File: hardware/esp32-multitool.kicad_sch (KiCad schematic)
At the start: 0 parts

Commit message: block refactoring
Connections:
- no-connect marks 2 -> 0
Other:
- sheet analog_io renamed analog_in
- sheet digital_io renamed digital_in
- sheet 1wire ports: added 1WIRE_3V3, 1WIRE_DQ; removed none
- sheet analog_in ports: added AIN1, AIN2; removed none
- sheet canbus ports: added none; removed +3.3V, CAN_RX, CAN_TX, GND, VIN
- sheet digital_in ports: added DIN1, DIN2; removed none
- sheet esp32 ports: added 1WIRE_DQ, AIN1, AIN2, DIN1, DIN2, I2C_SCL, I2C_SDA, PWM1; removed CAN_RX, CAN_TX, GND, LEDC1
- sheet i2c ports: added I2C_3V3, I2C_GND, I2C_SCL, I2C_SDA; removed none
- sheet power: file power.kicad_sch -> blocks/AOZ1280CI/AOZ1280CI.kicad_sch
- sheet power ports: added VIN_PROTECTED; removed +3.3V, GND, USB_5V, VIN
- sheet pwm ports: added PWM1, VIN_PROTECTED; removed none

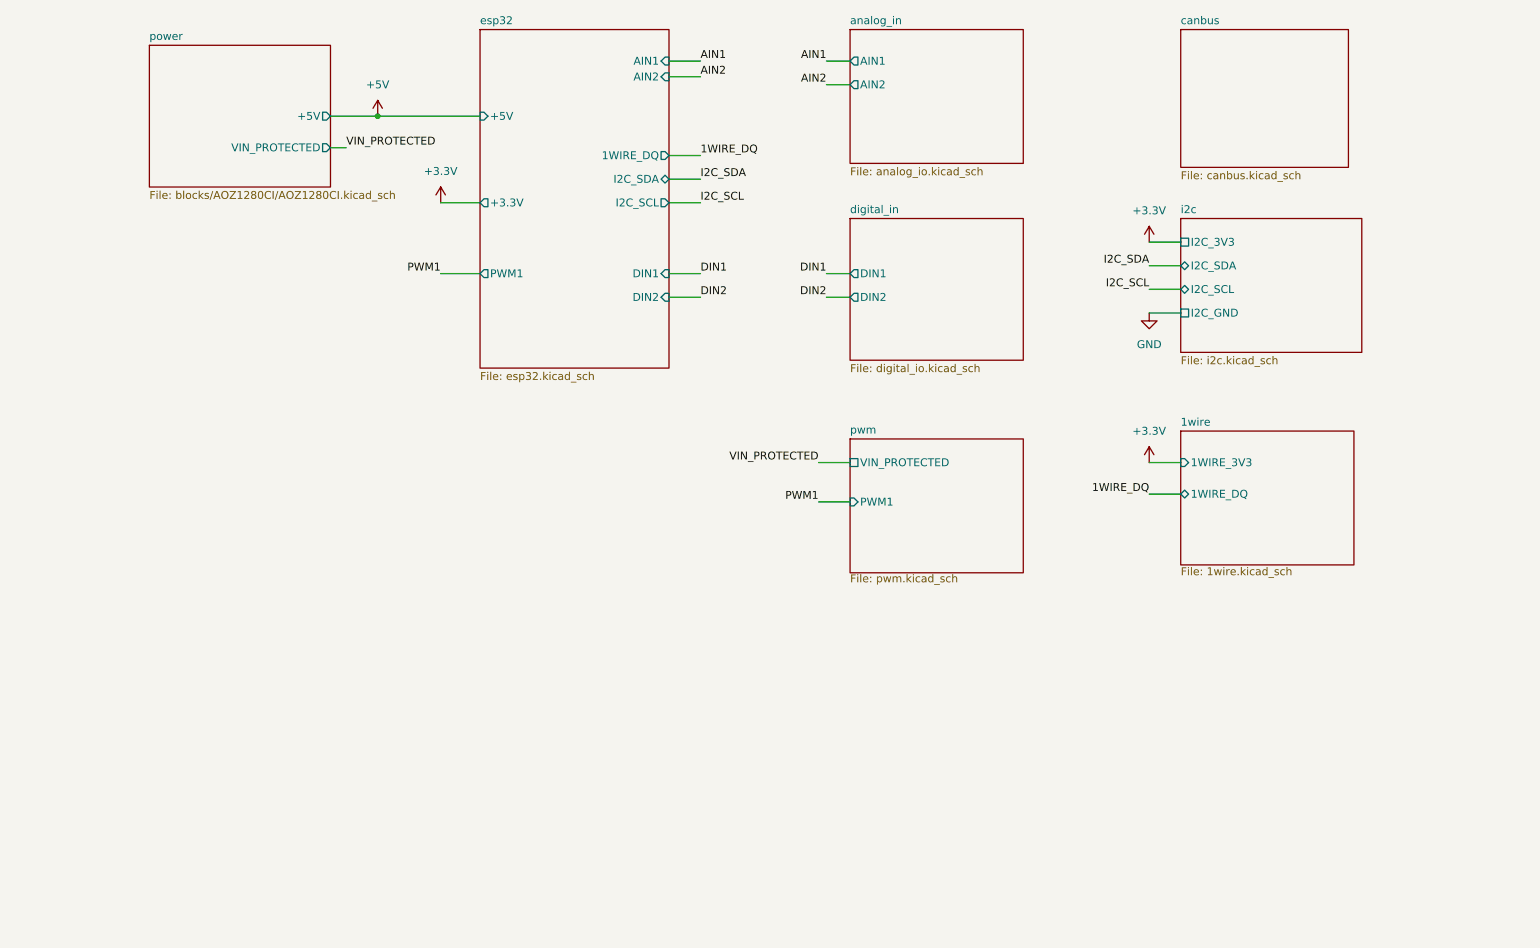
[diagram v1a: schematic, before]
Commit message: Added 3D models and ran freerouting
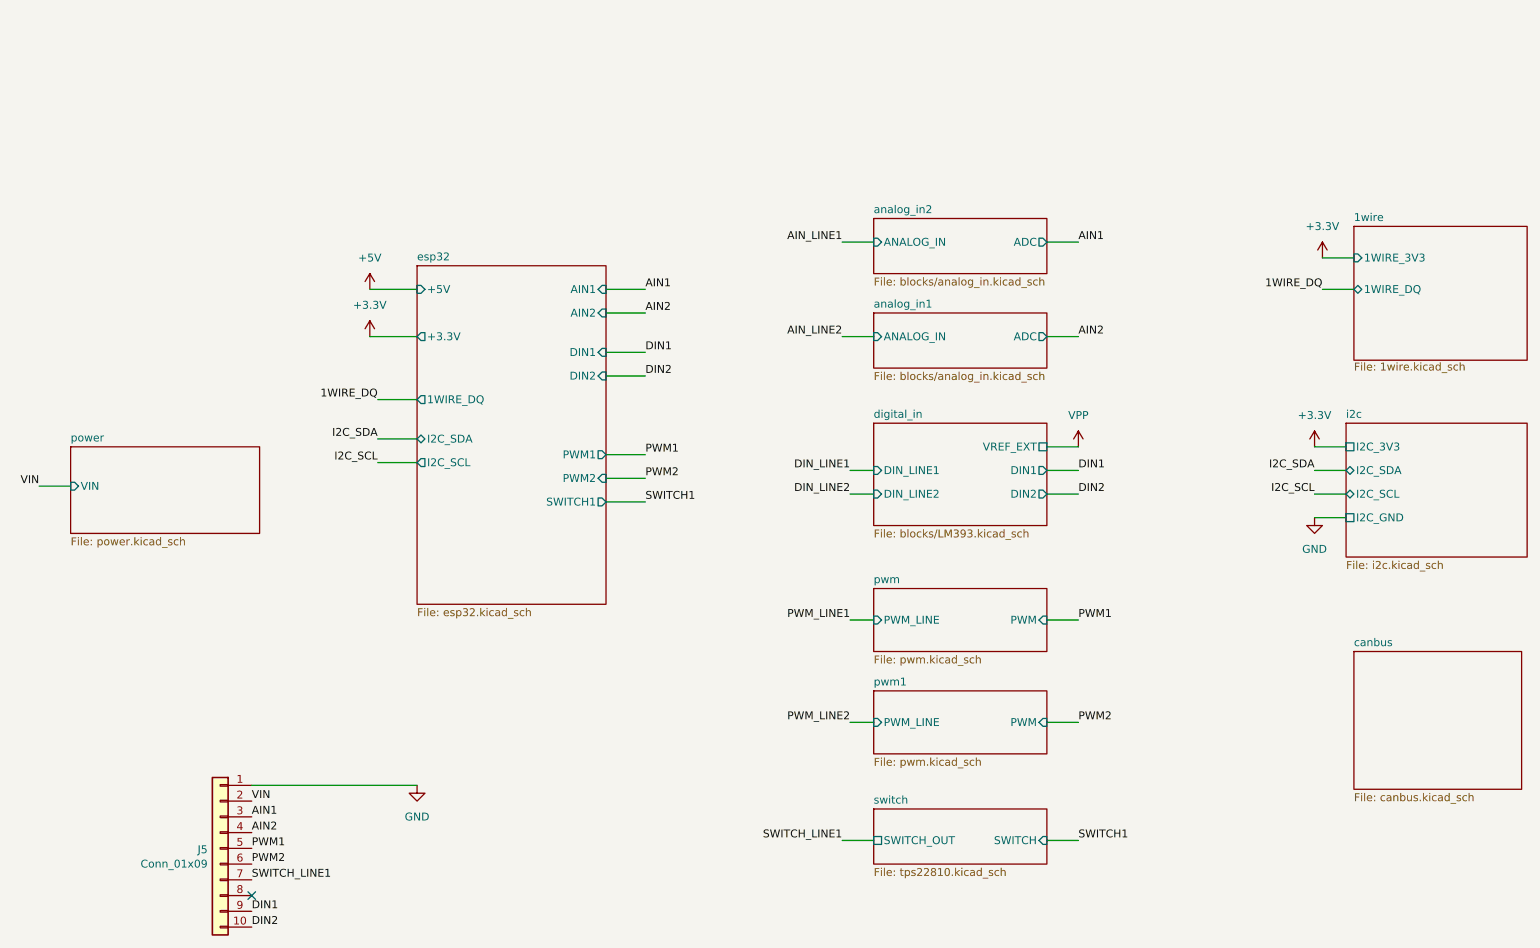
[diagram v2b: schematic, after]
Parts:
- added J5: Conn_01x09, TerminalBlock_Phoenix:TerminalBlock_Phoenix_MPT-0,5-10-2.54_1x10_P2.54mm_Horizontal, symbol Connector_Generic:Conn_01x10
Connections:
- net AIN1: now also J5.3 (Pin_3)
- net AIN2: now also J5.4 (Pin_4)
- net DIN1: now also J5.9 (Pin_9)
- net DIN2: now also J5.10 (Pin_10)
- net GND: now also J5.1 (Pin_1)
- net PWM1: now also J5.5 (Pin_5)
- new net PWM2: J5.6 (Pin_6)
- new net SWITCH_LINE1: J5.7 (Pin_7)
- new net VIN: J5.2 (Pin_2)
- no-connect marks 0 -> 1
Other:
- sheet analog_in renamed analog_in1
- added sheet analog_in2 (blocks/analog_in.kicad_sch)
- added sheet pwm1 (pwm.kicad_sch)
- added sheet switch (tps22810.kicad_sch)
- sheet analog_in1: file analog_io.kicad_sch -> blocks/analog_in.kicad_sch
- sheet analog_in1 ports: added ADC, ANALOG_IN; removed AIN1, AIN2
- sheet digital_in: file digital_io.kicad_sch -> blocks/LM393.kicad_sch
- sheet digital_in ports: added DIN_LINE1, DIN_LINE2, VREF_EXT; removed none
- sheet esp32 ports: added PWM2, SWITCH1; removed none
- sheet power: file blocks/AOZ1280CI/AOZ1280CI.kicad_sch -> power.kicad_sch
- sheet power ports: added VIN; removed +5V, VIN_PROTECTED
- sheet pwm ports: added PWM, PWM_LINE; removed PWM1, VIN_PROTECTED
